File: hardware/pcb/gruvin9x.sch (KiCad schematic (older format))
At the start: 257 parts, among them IC1 ATMEGA2560-A_GRUVIN, J1 JUMPER_2W, J4 JUMPER_2W, K1 CONN_3, K2 CONN_3, K3 CONN_3, K4 CONN_5, K5 CONN_3, K6 CONN_3, P1 CONN_3X2, P10 CONN_5X2, P12 CONN_4, P13 CONN_8, P14 CONN_2, P15 CONN_4, P18 CONN_2, P2 CONN_5, P20 CONN_8, P21 CONN_3, P23 CONN_1, P24 CONN_1, P25 CONN_1, P26 CONN_1, P3 CONN_6, P4 CONN_9, P5 CONN_9, P6 CONN_6, P7 CONN_12, P8 CONN_30_LCD_GRUVIN, P9 CONN_1, Q1 BC847C, Q10 Si2319DS, Q2 BC847C, Q3 BC857C, Q4 BC847C, Q5 BC847C, Q6 Si2319DS, Q7 BC847C, Q8 BC847C, Q9 BC847C, SW1 SW_PUSH, SW2 SW_PUSH, SW3 SW_PUSH, SW4 SW_PUSH, SW5 SW_PUSH, SW6 SW_PUSH, U1 78L05, U2 78L05, U3 LN-6206-30, U4 TPS77601, U5 REF3012, X1 16MHz

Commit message: Main PCB version bumped to v4.2. Changes to pseudo RS-232 buffer circuit around Q2 and Q3.
Changes (tested) have been made to imporve output waveform shapes at higher
baudrates, such as that used for DSM2 (125,000 Baud.) This only affects the use
of the pseudo RS-232 output, as opposed to the TTL output. This is desired when
both Fr-Sky and DSM2 external plug-in modules are used and one doesn't want to
have to modify the Fr-Sky module internally. In other words, both modules can
be operated off the same (pseudo) RS-232 TX.RX port. (The DSM2 module requires
an additional (preferably high-speed) transistor to re-invert and level shift 
serial data to 3.3V TTL. Gruvin got away with a carefully biased/shunted, 
general purpose BC847C ... but only just.
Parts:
- added R117: 1K, symbol R
- R69, R72, R74: value 10K -> 5K1
- R73: value 10K -> 1K
- R76: value 10K -> 3K9
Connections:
- wire segments 717 -> 720
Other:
- moved on the sheet: R73
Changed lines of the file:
@@
-EESchema Schematic File Version 2  date 21/12/2011 7:18:59 a.m.
+EESchema Schematic File Version 2  date 15/02/2012 9:06:26 p.m.
 LIBS:device
 LIBS:transistors
@@
 Sheet 1 1
 Title "Main Controller PCB for 100pin ATMega"
-Date "20 dec 2011"
-Rev "4.1"
+Date "15 feb 2012"
+Rev "4.2"
 Comp ""
 Comment1 ""
@@
 Comment4 "Licensed under the TAPR Open Hardware License (see file,  LICENSE)"
 $EndDescr
-Text Label 12700 10200 0    60   ~ 0
-BATT+_FUSED
-Text Label 18650 12250 0    60   ~ 0
-BATT+_FUSED
+Connection ~ 11500 2050
+Wire Wire Line
+	11500 2050 11050 2050
+Wire Wire Line
+	11050 2050 11050 2150
 Wire Wire Line
 	18100 12250 17650 12250
 Wire Wire Line
-	18600 12250 19300 12250
+	19300 12250 18600 12250
 Wire Wire Line
 	12700 10200 13550 10200
@@
 	21850 9250 22450 9250
 Wire Wire Line
-	21300 10750 21300 10250
+	21300 10250 21300 10750
 Connection ~ 21050 9750
 Wire Wire Line
@@
 	22450 10050 22450 9750
 Wire Wire Line
-	21300 9750 20400 9750
+	20400 9750 21300 9750
 Wire Wire Line
 	19100 11650 18550 11650
@@
 Connection ~ 21350 12250
 Wire Wire Line
-	21450 12250 21300 12250
+	21300 12250 21450 12250
 Wire Wire Line
 	21950 12250 22250 12250
@@
 Connection ~ 21050 14200
 Wire Wire Line
-	21050 14350 21050 14000
+	21050 14000 21050 14350
 Connection ~ 20450 13700
 Wire Wire Line
 	20450 13800 20450 13700
 Wire Wire Line
-	10050 14400 10450 14400
+	10450 14400 10050 14400
 Wire Wire Line
-	15350 5450 15050 5450
+	15050 5450 15350 5450
 Wire Wire Line
-	15700 4700 14750 4700
+	14750 4700 15700 4700
 Wire Wire Line
-	14750 4900 15350 4900
+	15350 4900 14750 4900
 Wire Wire Line
 	5700 5400 5700 5450
@@
 	10250 13900 10250 13650
 Wire Wire Line
-	10850 13650 9000 13650
+	9000 13650 10850 13650
 Connection ~ 10450 13550
 Wire Wire Line
@@
 	6300 6200 5050 6200
 Wire Wire Line
-	6300 6000 5050 6000
+	5050 6000 6300 6000
 Wire Wire Line
 	6850 7200 6350 7200
@@
 	10650 11850 9000 11850
 Wire Wire Line
-	7450 8750 7450 7750
+	7450 7750 7450 8750
 Wire Wire Line
 	7550 8750 7550 7900
@@
 	14450 9700 14450 9850
 Wire Wire Line
-	14400 9850 14900 9850
+	14900 9850 14400 9850
 Wire Wire Line
 	11350 3050 11850 3050
 Wire Wire Line
-	11100 2750 11200 2750
+	10900 2750 11200 2750
 Wire Wire Line
-	11500 2550 11500 2500
+	11500 2550 11500 1950
 Wire Wire Line
 	13100 7350 12150 7350
@@
 	11750 3850 11950 3850
 Wire Wire Line
-	10200 2850 10200 2500
+	10200 2850 10200 1950
 Wire Wire Line
 	10200 3950 10200 4250
@@
 	10950 3750 10950 3850
 Wire Wire Line
-	11950 5100 10900 5100
+	10900 5100 11950 5100
 Wire Wire Line
 	17250 7750 17250 6100
@@
 	9350 3050 9350 3200
 Wire Wire Line
-	6000 2250 4350 2250
+	4350 2250 6000 2250
 Wire Wire Line
 	15800 8500 15800 8450
@@
 	7000 2400 7000 2250
 Wire Wire Line
-	7000 2950 7000 2800
+	7000 2800 7000 2950
 Wire Wire Line
 	7350 2800 7350 2900
@@
 	6400 2800 6400 2550
 Wire Wire Line
-	5500 2800 5500 2900
+	5500 2900 5500 2800
 Connection ~ 4800 2900
 Wire Wire Line
@@
 Connection ~ 4800 2250
 Wire Wire Line
-	4800 2250 4800 2400
+	4800 2400 4800 2250
 Wire Wire Line
 	5100 10850 4450 10850
@@
 Connection ~ 5150 2250
 Wire Wire Line
-	4800 2950 4800 2800
+	4800 2800 4800 2950
 Wire Wire Line
 	5500 3500 5500 3400
@@
 	18000 6800 19050 6800
 Wire Wire Line
-	17150 7650 17600 7650
+	17600 7650 17150 7650
 Connection ~ 17550 7650
 Wire Wire Line
@@
 	19100 8650 17300 8650
 Wire Wire Line
-	16700 9400 16100 9400
+	16100 9400 16700 9400
 Wire Wire Line
-	15800 9200 15800 9000
+	15800 9000 15800 9200
 Connection ~ 15800 9100
 Wire Wire Line
 	7650 2250 7650 2200
 Wire Wire Line
-	5500 2300 5500 2250
+	5500 2250 5500 2300
 Connection ~ 5500 2250
 Wire Wire Line
@@
 	11500 5200 11500 5300
 Wire Wire Line
-	10500 3750 11100 3750
+	11100 3750 10500 3750
 Wire Wire Line
-	10650 3850 10650 3750
+	10650 3750 10650 3850
 Connection ~ 10650 3750
 Wire Wire Line
@@
 Connection ~ 10800 4400
 Wire Wire Line
-	10200 3350 10200 3550
+	10200 3550 10200 3350
 Wire Wire Line
 	11600 3750 11950 3750
@@
 	13100 7150 12150 7150
 Wire Wire Line
-	12150 7650 13100 7650
+	13100 7650 12150 7650
 Wire Wire Line
-	18450 7100 16750 7100
+	16750 7100 18450 7100
 Wire Wire Line
 	13100 7450 12150 7450
@@
 	10800 3050 10850 3050
 Wire Wire Line
-	10600 2750 9900 2750
+	10400 2750 9900 2750
 Wire Wire Line
 	9900 2750 9900 4700
 Wire Wire Line
-	10900 5000 11950 5000
+	11950 5000 10900 5000
 Wire Wire Line
 	11850 3050 11850 3100
@@
 	11500 2950 11500 3050
 Wire Wire Line
-	16650 12650 16450 12650
+	16450 12650 16650 12650
 Connection ~ 16550 12650
 Wire Wire Line
@@
 	13950 8950 14000 8950
 Wire Wire Line
-	12150 7750 13100 7750
+	13100 7750 12150 7750
 Wire Wire Line
 	13900 9700 13850 9700
@@
 	13850 9650 13800 9650
 Wire Wire Line
-	7850 8500 7850 8750
+	7850 8750 7850 8500
 Wire Wire Line
 	8500 8550 8400 8550
@@
 	6700 5600 6700 5700
 Wire Wire Line
-	7750 14550 7450 14550
+	7450 14550 7750 14550
 Wire Wire Line
 	6400 13750 6050 13750
@@
 	5050 6100 5850 6100
 Wire Wire Line
-	6250 7100 5050 7100
+	5050 7100 6250 7100
 Wire Wire Line
 	6250 7300 5050 7300
@@
 	14500 15150 14500 15250
 Wire Wire Line
-	16050 15600 16050 14850
+	16050 14850 16050 15600
 Wire Wire Line
 	15800 14850 15800 14950
@@
 	11450 13550 11000 13550
 Wire Wire Line
-	10500 13550 9000 13550
+	9000 13550 10500 13550
 Wire Wire Line
 	11450 13650 11350 13650
 Connection ~ 10450 14400
 Wire Wire Line
-	9000 13750 10500 13750
+	10500 13750 9000 13750
 Connection ~ 10250 14400
 Wire Wire Line
@@
 Connection ~ 16600 9750
 Wire Wire Line
-	15800 9600 15800 10150
+	15800 10150 15800 9600
 Connection ~ 15800 10000
 Wire Wire Line
@@
 	4700 12250 4050 12250
 Wire Wire Line
-	20900 12550 20900 12800
+	20900 12800 20900 12550
 Wire Wire Line
-	18800 12250 18800 12550
+	18800 12550 18800 12250
 Wire Wire Line
 	22150 12350 22150 12650
@@
 Connection ~ 21150 8400
 Wire Wire Line
-	20700 8400 21650 8400
+	21650 8400 20700 8400
 Wire Wire Line
 	21150 8700 21150 8400
@@
 	22450 9250 22450 9350
 Wire Wire Line
-	17350 10950 19100 10950
+	19100 10950 17350 10950
 Wire Wire Line
-	17300 8850 19100 8850
+	19100 8850 17300 8850
 Wire Wire Line
 	21550 9550 20400 9550
@@
 	13000 10800 13550 10800
 Wire Wire Line
-	20500 12250 19700 12250
+	19700 12250 20500 12250
+Wire Wire Line
+	11050 2650 11050 2750
+Connection ~ 11050 2750
+$Comp
+L R R117
+U 1 1 4F3B625E
+P 11050 2400
+F 0 "R117" V 11130 2400 50  0000 C CNN
+F 1 "1K" V 11050 2400 50  0000 C CNN
+	1    11050 2400
+	1    0    0    -1
+$EndComp
+Text Label 12700 10200 0    60   ~ 0
+BATT+_FUSED
+Text Label 18650 12250 0    60   ~ 0
+BATT+_FUSED
 $Comp
 L CONN_5 K4
@@
 P 11100 3050
 F 0 "R76" V 11180 3050 50  0000 C CNN
-F 1 "10K" V 11100 3050 50  0000 C CNN
+F 1 "3K9" V 11100 3050 50  0000 C CNN
 	1    11100 3050
 	0    -1   -1   0
@@
 L R R73
 U 1 1 4CF47F1F
-P 10850 2750
-F 0 "R73" V 10930 2750 50  0000 C CNN
-F 1 "10K" V 10850 2750 50  0000 C CNN
-	1    10850 2750
+P 10650 2750
+F 0 "R73" V 10730 2750 50  0000 C CNN
+F 1 "1K" V 10650 2750 50  0000 C CNN
+	1    10650 2750
 	0    1    1    0
 $EndComp
@@
 L VCC #PWR053
 U 1 1 4CF47EF5
-P 11500 2500
-F 0 "#PWR053" H 11500 2600 30  0001 C CNN
-F 1 "VCC" H 11500 2600 30  0000 C CNN
-	1    11500 2500
+P 11500 1950
+F 0 "#PWR053" H 11500 2050 30  0001 C CNN
+F 1 "VCC" H 11500 2050 30  0000 C CNN
+	1    11500 1950
 	1    0    0    -1
 $EndComp
@@
 L VCC #PWR056
 U 1 1 4CEE0833
-P 10200 2500
-F 0 "#PWR056" H 10200 2600 30  0001 C CNN
-F 1 "VCC" H 10200 2600 30  0000 C CNN
-	1    10200 2500
+P 10200 1950
+F 0 "#PWR056" H 10200 2050 30  0001 C CNN
+F 1 "VCC" H 10200 2050 30  0000 C CNN
+	1    10200 1950
 	1    0    0    -1
 $EndComp
@@
 P 11350 3750
 F 0 "R74" V 11430 3750 50  0000 C CNN
-F 1 "10K" V 11350 3750 50  0000 C CNN
+F 1 "5K1" V 11350 3750 50  0000 C CNN
 	1    11350 3750
 	0    1    1    0
@@
 P 10950 4100
 F 0 "R72" V 11030 4100 50  0000 C CNN
-F 1 "10K" V 10950 4100 50  0000 C CNN
+F 1 "5K1" V 10950 4100 50  0000 C CNN
 	1    10950 4100
 	1    0    0    -1
@@
 P 10200 3100
 F 0 "R69" V 10280 3100 50  0000 C CNN
-F 1 "10K" V 10200 3100 50  0000 C CNN
+F 1 "5K1" V 10200 3100 50  0000 C CNN
 	1    10200 3100
 	1    0    0    -1

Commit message: trunk: Main PCB - BOM file and readme updated to current v4.2 status.
(Thanks for the reminder Cam. I'd forget to thingyjig, if it weren't screwed on!)

This included normalising all resitor/capacitor/inductor part values to
Japanese "5K1" format -- mainly so that the new (and much better!) KiCAD BOM
output remains reational and easy to compare to our BOM spreadsheet.
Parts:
- C1, C11: value 10uF -> 10u
- C10, C15, C17, C19, C2, C20, C21, C22, C23, C24, C25, C26, C27, C28, C29, C3, C30, C33, C34, C36, C37, C38, C39, C4, C40, C41, C42, C43, C5, C53, C54, C55, C56, C57, C58, C59, C6, C60, C61, C63, C64, C7, C8, C9, C91, C92, C93, C94, C95, C96: value 0.1uF -> 0u1
- C12, C18, C31, C35: value 47uF -> 47u
- C13, C14: value 18pF -> 18p
- C16, C44, C45, C46, C47, C48, C49, C50, C51, C52, C62: value 1uF -> 1u
- C32: value 22uF -> 22u
- D2: value 5.1v -> 5V1
- D3, D4: value 3.6v -> 3V6
- L1, L2: value 10uH -> 10u
- R103: value 1k -> 1K
- R106: value 1.5K -> 1K5
- R107, R108, R109, R110: value 5.1K -> 5K1
- R115: value 100k -> 100K

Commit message: MAIN PCB v4.2 -- Changes to PORTH header.
I have successfully changed the PORTH header from 8-pin to 10-pin and connected
GND/VCC to the extra pins. I also rotated the module so that pin-1 is now on
GND, rather than PH7. 

GND is on pad 1
VCC is on pad 2
PH0 to PH7 are on pads 3 through 10, respectively.
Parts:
- P20: symbol CONN_8 -> CONN_10
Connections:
- wire segments 720 -> 723
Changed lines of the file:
@@
-EESchema Schematic File Version 2  date 16/02/2012 11:20:25 p.m.
+EESchema Schematic File Version 2  date 2/04/2012 10:46:05 a.m.
 LIBS:device
 LIBS:transistors
@@
 Sheet 1 1
 Title "Main Controller PCB for 100pin ATMega"
-Date "16 feb 2012"
+Date "1 apr 2012"
 Rev "4.2"
 Comp ""
@@
 Comment4 "Licensed under the TAPR Open Hardware License (see file,  LICENSE)"
 $EndDescr
+Wire Wire Line
+	3850 12200 3850 12550
+Wire Wire Line
+	3850 12550 3550 12550
 Connection ~ 11500 2050
 Wire Wire Line
@@
 	18100 12250 17650 12250
 Wire Wire Line
-	19300 12250 18600 12250
+	18600 12250 19300 12250
 Wire Wire Line
 	12700 10200 13550 10200
@@
 	21850 9250 22450 9250
 Wire Wire Line
-	21300 10250 21300 10750
+	21300 10750 21300 10250
 Connection ~ 21050 9750
 Wire Wire Line
@@
 	22450 10050 22450 9750
 Wire Wire Line
-	20400 9750 21300 9750
+	21300 9750 20400 9750
 Wire Wire Line
 	19100 11650 18550 11650
@@
 Connection ~ 21350 12250
 Wire Wire Line
-	21300 12250 21450 12250
+	21450 12250 21300 12250
 Wire Wire Line
 	21950 12250 22250 12250
@@
 Connection ~ 21050 14200
 Wire Wire Line
-	21050 14000 21050 14350
+	21050 14350 21050 14000
 Connection ~ 20450 13700
 Wire Wire Line
 	20450 13800 20450 13700
 Wire Wire Line
-	10450 14400 10050 14400
+	10050 14400 10450 14400
 Wire Wire Line
-	15050 5450 15350 5450
+	15350 5450 15050 5450
 Wire Wire Line
-	14750 4700 15700 4700
+	15700 4700 14750 4700
 Wire Wire Line
-	15350 4900 14750 4900
+	14750 4900 15350 4900
 Wire Wire Line
 	5700 5400 5700 5450
@@
 	5700 7050 5700 7100
 Wire Wire Line
-	4650 13250 6400 13250
+	3550 13250 6400 13250
 Wire Wire Line
-	4650 13050 6400 13050
+	3550 13050 6400 13050
 Wire Wire Line
-	4650 12850 6400 12850
+	3550 12850 6400 12850
 Wire Wire Line
-	4650 12650 6400 12650
+	3550 12650 6400 12650
 Wire Wire Line
 	15700 4800 15350 4800
@@
 	10250 13900 10250 13650
 Wire Wire Line
-	9000 13650 10850 13650
+	10850 13650 9000 13650
 Connection ~ 10450 13550
 Wire Wire Line
@@
 	6300 6200 5050 6200
 Wire Wire Line
-	5050 6000 6300 6000
+	6300 6000 5050 6000
 Wire Wire Line
 	6850 7200 6350 7200
@@
 	10650 11850 9000 11850
 Wire Wire Line
-	7450 7750 7450 8750
+	7450 8750 7450 7750
 Wire Wire Line
 	7550 8750 7550 7900
@@
 	14450 9700 14450 9850
 Wire Wire Line
-	14900 9850 14400 9850
+	14400 9850 14900 9850
 Wire Wire Line
 	11350 3050 11850 3050
 Wire Wire Line
-	10900 2750 11200 2750
+	11200 2750 10900 2750
 Wire Wire Line
-	11500 2550 11500 1950
+	11500 1950 11500 2550
 Wire Wire Line
 	13100 7350 12150 7350
@@
 	10950 3750 10950 3850
 Wire Wire Line
-	10900 5100 11950 5100
+	11950 5100 10900 5100
 Wire Wire Line
 	17250 7750 17250 6100
@@
 	9350 3050 9350 3200
 Wire Wire Line
-	4350 2250 6000 2250
+	6000 2250 4350 2250
 Wire Wire Line
 	15800 8500 15800 8450
@@
 	7000 2400 7000 2250
 Wire Wire Line
-	7000 2800 7000 2950
+	7000 2950 7000 2800
 Wire Wire Line
 	7350 2800 7350 2900
@@
 	6400 2800 6400 2550
 Wire Wire Line
-	5500 2900 5500 2800
+	5500 2800 5500 2900
 Connection ~ 4800 2900
 Wire Wire Line
@@
 Connection ~ 4800 2250
 Wire Wire Line
-	4800 2400 4800 2250
+	4800 2250 4800 2400
 Wire Wire Line
 	5100 10850 4450 10850
@@
 Connection ~ 5150 2250
 Wire Wire Line
-	4800 2800 4800 2950
+	4800 2950 4800 2800
 Wire Wire Line
 	5500 3500 5500 3400
@@
 	18000 6800 19050 6800
 Wire Wire Line
-	17600 7650 17150 7650
+	17150 7650 17600 7650
 Connection ~ 17550 7650
 Wire Wire Line
@@
 	19100 8650 17300 8650
 Wire Wire Line
-	16100 9400 16700 9400
+	16700 9400 16100 9400
 Wire Wire Line
-	15800 9000 15800 9200
+	15800 9200 15800 9000
 Connection ~ 15800 9100
 Wire Wire Line
 	7650 2250 7650 2200
 Wire Wire Line
-	5500 2250 5500 2300
+	5500 2300 5500 2250
 Connection ~ 5500 2250
 Wire Wire Line
@@
 	11500 5200 11500 5300
 Wire Wire Line
-	11100 3750 10500 3750
+	10500 3750 11100 3750
 Wire Wire Line
-	10650 3750 10650 3850
+	10650 3850 10650 3750
 Connection ~ 10650 3750
 Wire Wire Line
@@
 Connection ~ 10800 4400
 Wire Wire Line
-	10200 3550 10200 3350
+	10200 3350 10200 3550
 Wire Wire Line
 	11600 3750 11950 3750
@@
 	13100 7150 12150 7150
 Wire Wire Line
-	13100 7650 12150 7650
+	12150 7650 13100 7650
 Wire Wire Line
-	16750 7100 18450 7100
+	18450 7100 16750 7100
 Wire Wire Line
 	13100 7450 12150 7450
@@
 	9900 2750 9900 4700
 Wire Wire Line
-	11950 5000 10900 5000
+	10900 5000 11950 5000
 Wire Wire Line
 	11850 3050 11850 3100
@@
 	11500 2950 11500 3050
 Wire Wire Line
-	16450 12650 16650 12650
+	16650 12650 16450 12650
 Connection ~ 16550 12650
 Wire Wire Line
@@
 	13950 8950 14000 8950
 Wire Wire Line
-	13100 7750 12150 7750
+	12150 7750 13100 7750
 Wire Wire Line
 	13900 9700 13850 9700
@@
 	13850 9650 13800 9650
 Wire Wire Line
-	7850 8750 7850 8500
+	7850 8500 7850 8750
 Wire Wire Line
 	8500 8550 8400 8550
@@
 	6700 5600 6700 5700
 Wire Wire Line
-	7450 14550 7750 14550
+	7750 14550 7450 14550
 Wire Wire Line
 	6400 13750 6050 13750
@@
 	5050 6100 5850 6100
 Wire Wire Line
-	5050 7100 6250 7100
+	6250 7100 5050 7100
 Wire Wire Line
 	6250 7300 5050 7300
@@
 	14500 15150 14500 15250
 Wire Wire Line
-	16050 14850 16050 15600
+	16050 15600 16050 14850
 Wire Wire Line
 	15800 14850 15800 14950
@@
 	11450 13550 11000 13550
 Wire Wire Line
-	9000 13550 10500 13550
+	10500 13550 9000 13550
 Wire Wire Line
 	11450 13650 11350 13650
 Connection ~ 10450 14400
 Wire Wire Line
-	10500 13750 9000 13750
+	9000 13750 10500 13750
 Connection ~ 10250 14400
 Wire Wire Line
@@
 Connection ~ 16600 9750
 Wire Wire Line
-	15800 10150 15800 9600
+	15800 9600 15800 10150
 Connection ~ 15800 10000
 Wire Wire Line
@@
 	4700 12250 4050 12250
 Wire Wire Line
-	20900 12800 20900 12550
+	20900 12550 20900 12800
 Wire Wire Line
 	18800 12550 18800 12250
@@
 	15600 4900 15600 5050
 Wire Wire Line
-	4650 12750 6400 12750
+	3550 12750 6400 12750
 Wire Wire Line
-	4650 12950 6400 12950
+	3550 12950 6400 12950
 Wire Wire Line
-	6400 13150 4650 13150
+	6400 13150 3550 13150
 Wire Wire Line
-	4650 13350 6400 13350
+	3550 13350 6400 13350
 Wire Wire Line
 	5850 7200 5850 7050
@@
 Connection ~ 21150 8400
 Wire Wire Line
-	21650 8400 20700 8400
+	20700 8400 21650 8400
 Wire Wire Line
 	21150 8700 21150 8400
@@
 	22450 9250 22450 9350
 Wire Wire Line
-	19100 10950 17350 10950
+	17350 10950 19100 10950
 Wire Wire Line
-	19100 8850 17300 8850
+	17300 8850 19100 8850
 Wire Wire Line
 	21550 9550 20400 9550
@@
 	13000 10800 13550 10800
 Wire Wire Line
-	19700 12250 20500 12250
+	20500 12250 19700 12250
 Wire Wire Line
 	11050 2650 11050 2750
 Connection ~ 11050 2750
+Wire Wire Line
+	3550 12450 3700 12450
+$Comp
+L VCC #PWR?
+U 1 1 4F78DA94
+P 3850 12200
+F 0 "#PWR?" H 3850 12300 30  0001 C CNN
+F 1 "VCC" H 3850 12300 30  0000 C CNN
+	1    3850 12200
+	1    0    0    -1
+$EndComp
+$Comp
+L GND #PWR?
+U 1 1 4F78DA82
+P 3700 12450
+F 0 "#PWR?" H 3700 12450 30  0001 C CNN
+F 1 "GND" H 3700 12380 30  0001 C CNN
+	1    3700 12450
+	0    -1   -1   0
+$EndComp
 $Comp
 L R R117
@@
 Spare1\LED-BL-opt
 $Comp
-L CONN_8 P20
+L CONN_10 P20
 U 1 1 4DC18D59
-P 4300 13000
-F 0 "P20" V 4250 13000 60  0000 C CNN
-F 1 "CONN_8" V 4350 13000 60  0000 C CNN
-	1    4300 13000
-	-1   0    0    1
+P 3200 12900
+F 0 "P20" V 3150 12900 60  0000 C CNN
+F 1 "CONN_8" V 3250 12900 60  0000 C CNN
+	1    3200 12900
+	-1   0    0    -1
 $EndComp
 $Comp

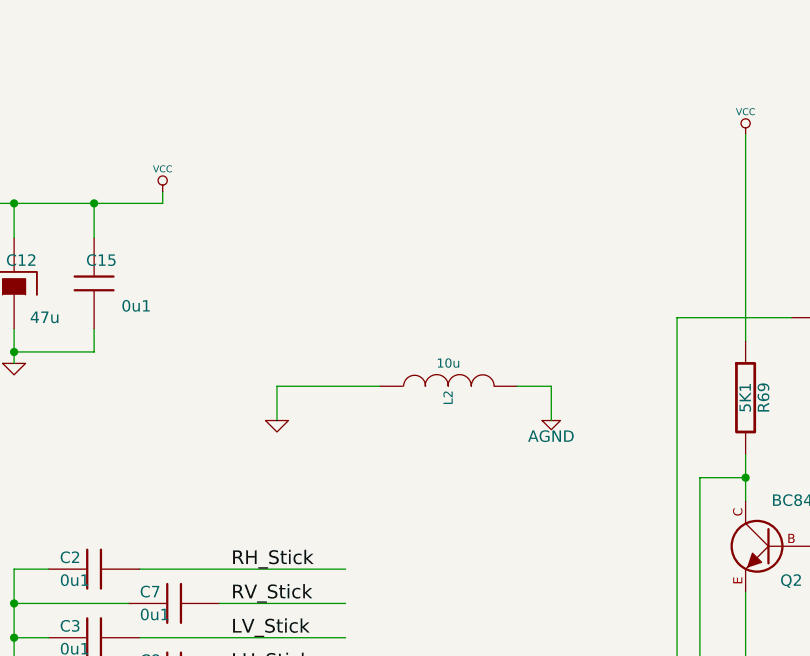
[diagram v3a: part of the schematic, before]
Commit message: MAIN BOARD v4.2 CHANGES -- PORTH (continued)
. Added C65 0u1 decoupling capactor for MCU pins 10 and 11.
. Changed PORTH VCC supply source to get it away from the MCU supply. 
  (Required less re-routing than expected. Always nice! :-D)
. Tidied up a few multi-segment tracks I came across while I was at it.
. Updated gruvin9x-readme.txt and gruvin9x-bom.xls to reflect the above.
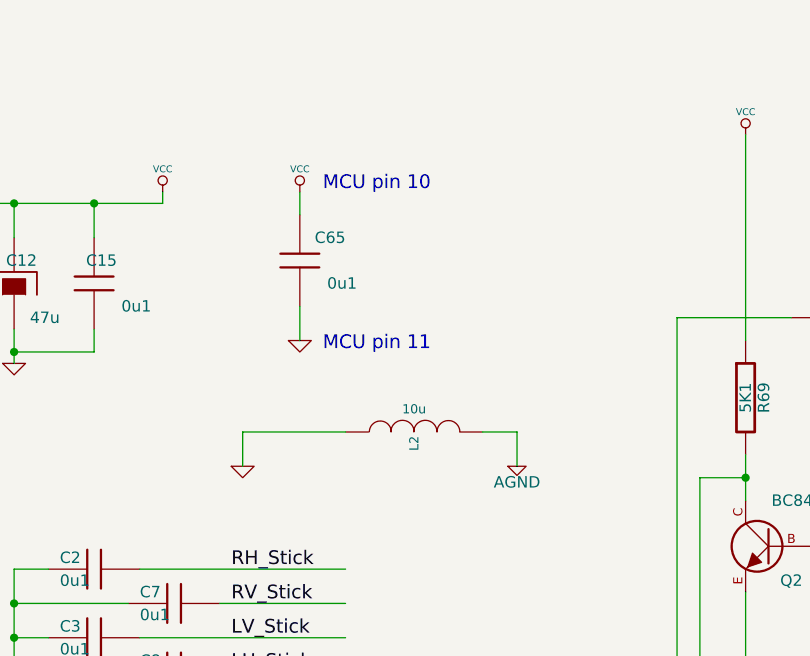
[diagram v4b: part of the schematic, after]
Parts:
- added C65: 0u1, symbol C
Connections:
- wire segments 723 -> 725
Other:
- note added: "MCU pin 10"
- note added: "MCU pin 11"
- moved on the sheet: L2
